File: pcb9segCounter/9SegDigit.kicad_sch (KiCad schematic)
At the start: 10 parts

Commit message: Making progress, figuring out microcontroller interfacing
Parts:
- renumbered D2 to D19, D3 to D20, D4 to D21, D5 to D22, D6 to D23, D7 to D24, D8 to D25, D9 to D26, D10 to D27, D1 to S3
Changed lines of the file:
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@@
 		(dnp no)
 		(fields_autoplaced yes)
-		(property "Reference" "D5"
+		(property "Reference" "D22"
 			(at 104.14 101.6314 0)
 			(effects
@@
 		(instances
 			(project "pcb9segCounter"
+				(path "/c50b0073-6340-498a-8f0c-212ef3b3c0fe/22bfc2a0-8fcb-4720-a36c-753b0c572d0f"
+					(reference "D22")
+					(unit 1)
+				)
+				(path "/c50b0073-6340-498a-8f0c-212ef3b3c0fe/3b31bf75-0830-4091-8274-a65747ea74f2"
+					(reference "D13")
+					(unit 1)
+				)
 				(path "/c50b0073-6340-498a-8f0c-212ef3b3c0fe/5c493882-1689-4a6d-b4b4-08608e8edf66"
-					(reference "D5")
+					(reference "D4")
+					(unit 1)
+				)
+				(path "/c50b0073-6340-498a-8f0c-212ef3b3c0fe/b6b935bf-feab-4172-8fa2-42984df36767"
+					(reference "D31")
 					(unit 1)
 				)
@@
 		(dnp no)
 		(fields_autoplaced yes)
-		(property "Reference" "D4"
+		(property "Reference" "D21"
 			(at 86.36 101.6314 0)
 			(effects
@@
 		(instances
 			(project "pcb9segCounter"
+				(path "/c50b0073-6340-498a-8f0c-212ef3b3c0fe/22bfc2a0-8fcb-4720-a36c-753b0c572d0f"
+					(reference "D21")
+					(unit 1)
+				)
+				(path "/c50b0073-6340-498a-8f0c-212ef3b3c0fe/3b31bf75-0830-4091-8274-a65747ea74f2"
+					(reference "D12")
+					(unit 1)
+				)
 				(path "/c50b0073-6340-498a-8f0c-212ef3b3c0fe/5c493882-1689-4a6d-b4b4-08608e8edf66"
-					(reference "D4")
+					(reference "D3")
+					(unit 1)
+				)
+				(path "/c50b0073-6340-498a-8f0c-212ef3b3c0fe/b6b935bf-feab-4172-8fa2-42984df36767"
+					(reference "D30")
 					(unit 1)
 				)
@@
 		(dnp no)
 		(fields_autoplaced yes)
-		(property "Reference" "D6"
+		(property "Reference" "D23"
 			(at 121.92 101.6314 0)
 			(effects
@@
 		(instances
 			(project "pcb9segCounter"
+				(path "/c50b0073-6340-498a-8f0c-212ef3b3c0fe/22bfc2a0-8fcb-4720-a36c-753b0c572d0f"
+					(reference "D23")
+					(unit 1)
+				)
+				(path "/c50b0073-6340-498a-8f0c-212ef3b3c0fe/3b31bf75-0830-4091-8274-a65747ea74f2"
+					(reference "D14")
+					(unit 1)
+				)
 				(path "/c50b0073-6340-498a-8f0c-212ef3b3c0fe/5c493882-1689-4a6d-b4b4-08608e8edf66"
-					(reference "D6")
+					(reference "D5")
+					(unit 1)
+				)
+				(path "/c50b0073-6340-498a-8f0c-212ef3b3c0fe/b6b935bf-feab-4172-8fa2-42984df36767"
+					(reference "D32")
 					(unit 1)
 				)
@@
 		(dnp no)
 		(fields_autoplaced yes)
-		(property "Reference" "D3"
+		(property "Reference" "D20"
 			(at 68.58 101.6314 0)
 			(effects
@@
 		(instances
 			(project "pcb9segCounter"
+				(path "/c50b0073-6340-498a-8f0c-212ef3b3c0fe/22bfc2a0-8fcb-4720-a36c-753b0c572d0f"
+					(reference "D20")
+					(unit 1)
+				)
+				(path "/c50b0073-6340-498a-8f0c-212ef3b3c0fe/3b31bf75-0830-4091-8274-a65747ea74f2"
+					(reference "D11")
+					(unit 1)
+				)
 				(path "/c50b0073-6340-498a-8f0c-212ef3b3c0fe/5c493882-1689-4a6d-b4b4-08608e8edf66"
-					(reference "D3")
+					(reference "D2")
+					(unit 1)
+				)
+				(path "/c50b0073-6340-498a-8f0c-212ef3b3c0fe/b6b935bf-feab-4172-8fa2-42984df36767"
+					(reference "D29")
 					(unit 1)
 				)
@@
 		(on_board yes)
 		(dnp no)
-		(property "Reference" "D2"
+		(property "Reference" "D19"
 			(at 47.752 99.314 0)
 			(effects
@@
 		(instances
 			(project "pcb9segCounter"
+				(path "/c50b0073-6340-498a-8f0c-212ef3b3c0fe/22bfc2a0-8fcb-4720-a36c-753b0c572d0f"
+					(reference "D19")
+					(unit 1)
+				)
+				(path "/c50b0073-6340-498a-8f0c-212ef3b3c0fe/3b31bf75-0830-4091-8274-a65747ea74f2"
+					(reference "D10")
+					(unit 1)
+				)
 				(path "/c50b0073-6340-498a-8f0c-212ef3b3c0fe/5c493882-1689-4a6d-b4b4-08608e8edf66"
-					(reference "D2")
+					(reference "D1")
+					(unit 1)
+				)
+				(path "/c50b0073-6340-498a-8f0c-212ef3b3c0fe/b6b935bf-feab-4172-8fa2-42984df36767"
+					(reference "D28")
 					(unit 1)
 				)
@@
 		(dnp no)
 		(fields_autoplaced yes)
-		(property "Reference" "D7"
+		(property "Reference" "D24"
 			(at 139.7 101.6314 0)
 			(effects
@@
 		(instances
 			(project "pcb9segCounter"
+				(path "/c50b0073-6340-498a-8f0c-212ef3b3c0fe/22bfc2a0-8fcb-4720-a36c-753b0c572d0f"
+					(reference "D24")
+					(unit 1)
+				)
+				(path "/c50b0073-6340-498a-8f0c-212ef3b3c0fe/3b31bf75-0830-4091-8274-a65747ea74f2"
+					(reference "D15")
+					(unit 1)
+				)
 				(path "/c50b0073-6340-498a-8f0c-212ef3b3c0fe/5c493882-1689-4a6d-b4b4-08608e8edf66"
-					(reference "D7")
+					(reference "D6")
+					(unit 1)
+				)
+				(path "/c50b0073-6340-498a-8f0c-212ef3b3c0fe/b6b935bf-feab-4172-8fa2-42984df36767"
+					(reference "D33")
 					(unit 1)
 				)
@@
 		(dnp no)
 		(fields_autoplaced yes)
-		(property "Reference" "D1"
+		(property "Reference" "S3"
 			(at 101.6 76.8349 0)
 			(effects
@@
 		(instances
 			(project "pcb9segCounter"
+				(path "/c50b0073-6340-498a-8f0c-212ef3b3c0fe/22bfc2a0-8fcb-4720-a36c-753b0c572d0f"
+					(reference "S3")
+					(unit 1)
+				)
+				(path "/c50b0073-6340-498a-8f0c-212ef3b3c0fe/3b31bf75-0830-4091-8274-a65747ea74f2"
+					(reference "S2")
+					(unit 1)
+				)
 				(path "/c50b0073-6340-498a-8f0c-212ef3b3c0fe/5c493882-1689-4a6d-b4b4-08608e8edf66"
-					(reference "D1")
+					(reference "S1")
+					(unit 1)
+				)
+				(path "/c50b0073-6340-498a-8f0c-212ef3b3c0fe/b6b935bf-feab-4172-8fa2-42984df36767"
+					(reference "S4")
 					(unit 1)
 				)
@@
 		(dnp no)
 		(fields_autoplaced yes)
-		(property "Reference" "D10"
+		(property "Reference" "D27"
 			(at 193.04 101.6314 0)
 			(effects
@@
 		(instances
 			(project "pcb9segCounter"
+				(path "/c50b0073-6340-498a-8f0c-212ef3b3c0fe/22bfc2a0-8fcb-4720-a36c-753b0c572d0f"
+					(reference "D27")
+					(unit 1)
+				)
+				(path "/c50b0073-6340-498a-8f0c-212ef3b3c0fe/3b31bf75-0830-4091-8274-a65747ea74f2"
+					(reference "D18")
+					(unit 1)
+				)
 				(path "/c50b0073-6340-498a-8f0c-212ef3b3c0fe/5c493882-1689-4a6d-b4b4-08608e8edf66"
-					(reference "D10")
+					(reference "D9")
+					(unit 1)
+				)
+				(path "/c50b0073-6340-498a-8f0c-212ef3b3c0fe/b6b935bf-feab-4172-8fa2-42984df36767"
+					(reference "D36")
 					(unit 1)
 				)
@@
 		(dnp no)
 		(fields_autoplaced yes)
-		(property "Reference" "D8"
+		(property "Reference" "D25"
 			(at 157.48 101.6314 0)
 			(effects
@@
 		(instances
 			(project "pcb9segCounter"
+				(path "/c50b0073-6340-498a-8f0c-212ef3b3c0fe/22bfc2a0-8fcb-4720-a36c-753b0c572d0f"
+					(reference "D25")
+					(unit 1)
+				)
+				(path "/c50b0073-6340-498a-8f0c-212ef3b3c0fe/3b31bf75-0830-4091-8274-a65747ea74f2"
+					(reference "D16")
+					(unit 1)
+				)
 				(path "/c50b0073-6340-498a-8f0c-212ef3b3c0fe/5c493882-1689-4a6d-b4b4-08608e8edf66"
-					(reference "D8")
+					(reference "D7")
+					(unit 1)
+				)
+				(path "/c50b0073-6340-498a-8f0c-212ef3b3c0fe/b6b935bf-feab-4172-8fa2-42984df36767"
+					(reference "D34")
 					(unit 1)
 				)
@@
 		(dnp no)
 		(fields_autoplaced yes)
-		(property "Reference" "D9"
+		(property "Reference" "D26"
 			(at 175.26 101.6314 0)
 			(effects
@@
 		(instances
 			(project "pcb9segCounter"
+				(path "/c50b0073-6340-498a-8f0c-212ef3b3c0fe/22bfc2a0-8fcb-4720-a36c-753b0c572d0f"
+					(reference "D26")
+					(unit 1)
+				)
+				(path "/c50b0073-6340-498a-8f0c-212ef3b3c0fe/3b31bf75-0830-4091-8274-a65747ea74f2"
+					(reference "D17")
+					(unit 1)
+				)
 				(path "/c50b0073-6340-498a-8f0c-212ef3b3c0fe/5c493882-1689-4a6d-b4b4-08608e8edf66"
-					(reference "D9")
-					(unit 1)
-				)
+					(reference "D8")
+					(unit 1)
+				)
+				(path "/c50b0073-6340-498a-8f0c-212ef3b3c0fe/b6b935bf-feab-4172-8fa2-42984df36767"
+					(reference "D35")
+					(unit 1)
+				)

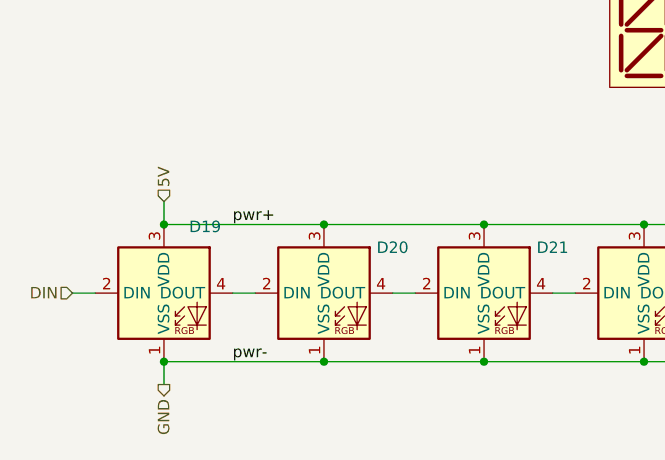
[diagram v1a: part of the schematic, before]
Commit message: Schematic looks good, going to branch to reduce the number of digits from 4 to 2
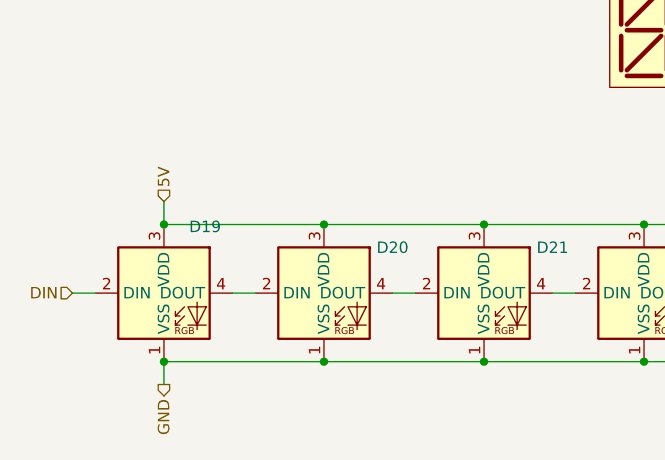
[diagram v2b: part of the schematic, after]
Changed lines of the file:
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@@
-		)
-	)
-	(label "pwr+"
-		(at 50.8 99.06 0)
-		(fields_autoplaced yes)
-		(effects
-			(font
-				(size 1.27 1.27)
-			)
-			(justify left bottom)
-		)
-	)
-	(label "pwr-"
-		(at 50.8 114.3 0)
-		(fields_autoplaced yes)
-		(effects
-			(font
-				(size 1.27 1.27)
-			)
-			(justify left bottom)
 		)
 	)

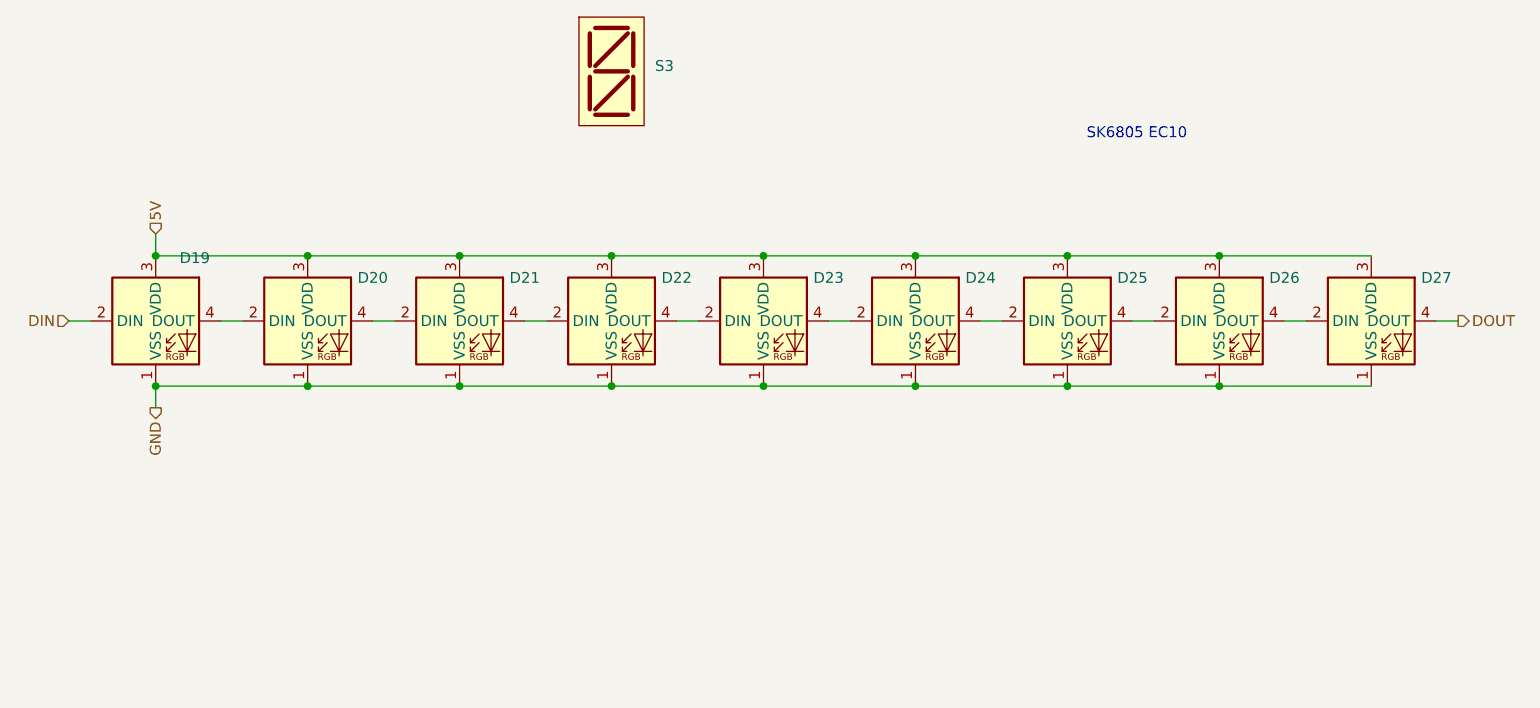
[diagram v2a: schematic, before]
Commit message: reduced to 2 digits, added capacitors
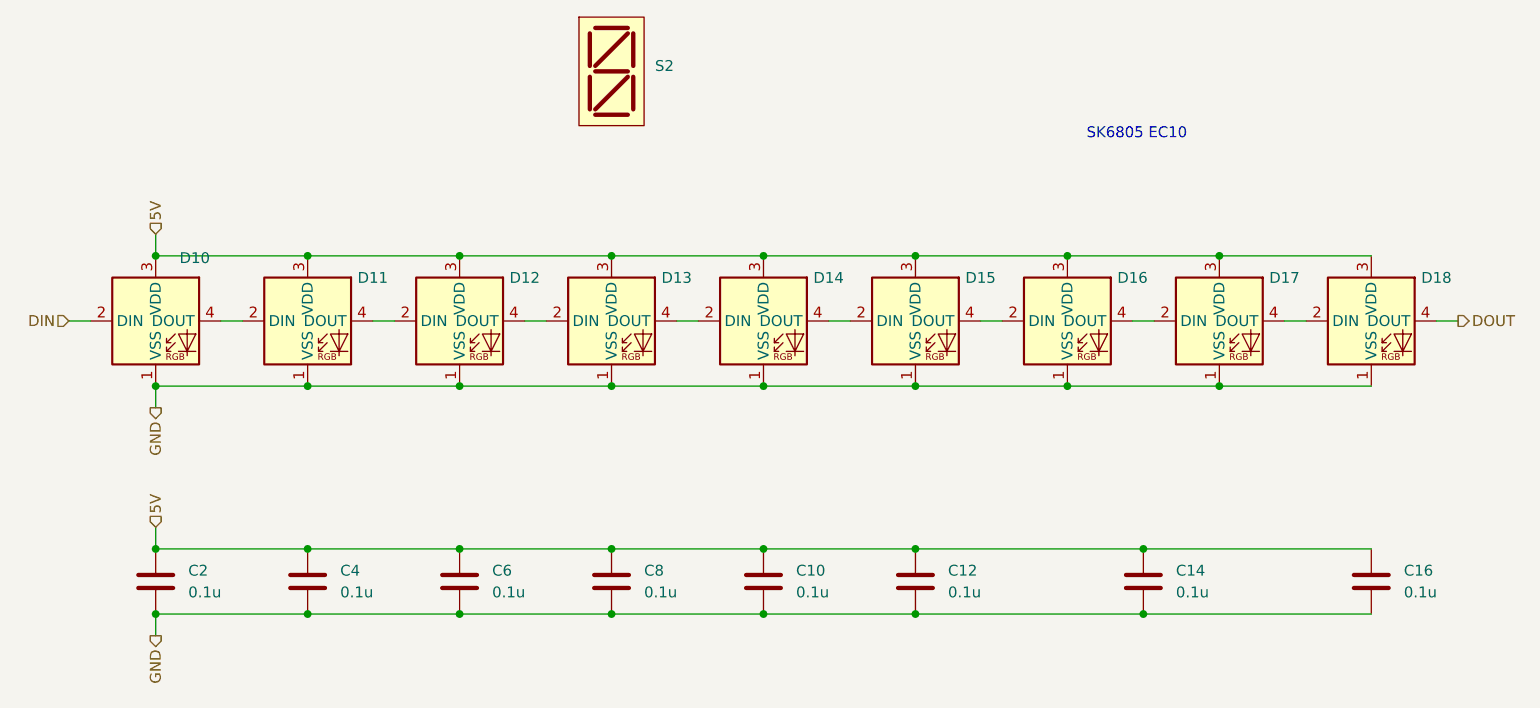
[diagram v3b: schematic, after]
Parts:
- added C10, C12, C14, C16, C2, C4, C6, C8: 0.1u, Capacitor_SMD:C_0805_2012Metric, symbol Device:C
- renumbered D19 to D10, D20 to D11, D21 to D12, D22 to D13, D23 to D14, D24 to D15, D25 to D16, D26 to D17, D27 to D18, S3 to S2
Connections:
- net 5V: now also C10.1, C12.1, C14.1, C16.1, C2.1, C4.1, C6.1, C8.1
- net GND: now also C10.2, C12.2, C14.2, C16.2, C2.2, C4.2, C6.2, C8.2

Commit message: good routing, need to add slikscreen details
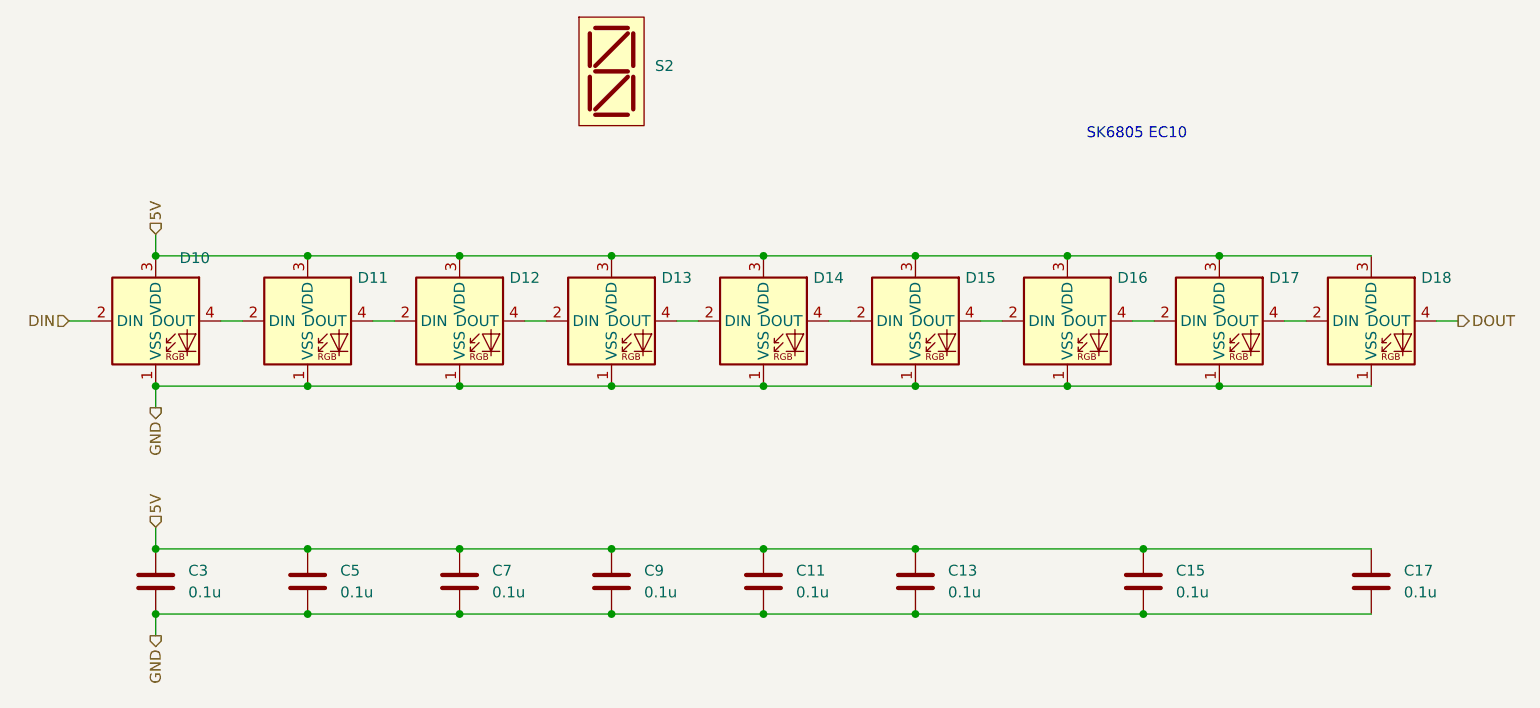
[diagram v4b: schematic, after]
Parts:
- renumbered C10 to C11, C12 to C13, C14 to C15, C16 to C17, C2 to C3, C4 to C5, C6 to C7, C8 to C9
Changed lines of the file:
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@@
 		(on_board yes)
 		(dnp no)
-		(property "Reference" "C2"
+		(property "Reference" "C3"
 			(at 46.99 135.8899 0)
 			(effects
@@
 		(dnp no)
 		(fields_autoplaced yes)
-		(property "Reference" "C14"
+		(property "Reference" "C15"
 			(at 162.56 135.8899 0)
 			(effects
@@
 		(dnp no)
 		(fields_autoplaced yes)
-		(property "Reference" "C10"
+		(property "Reference" "C11"
 			(at 118.11 135.8899 0)
 			(effects
@@
 		(dnp no)
 		(fields_autoplaced yes)
-		(property "Reference" "C12"
+		(property "Reference" "C13"
 			(at 135.89 135.8899 0)
 			(effects
@@
 		(dnp no)
 		(fields_autoplaced yes)
-		(property "Reference" "C4"
+		(property "Reference" "C5"
 			(at 64.77 135.8899 0)
 			(effects
@@
 		(dnp no)
 		(fields_autoplaced yes)
-		(property "Reference" "C16"
+		(property "Reference" "C17"
 			(at 189.23 135.8899 0)
 			(effects
@@
 		(dnp no)
 		(fields_autoplaced yes)
-		(property "Reference" "C6"
+		(property "Reference" "C7"
 			(at 82.55 135.8899 0)
 			(effects
@@
 		(dnp no)
 		(fields_autoplaced yes)
-		(property "Reference" "C8"
+		(property "Reference" "C9"
 			(at 100.33 135.8899 0)
 			(effects

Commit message: Looks really good, all footprints and implementation check out. Looking to move an LED and adding an additional decap capacitor
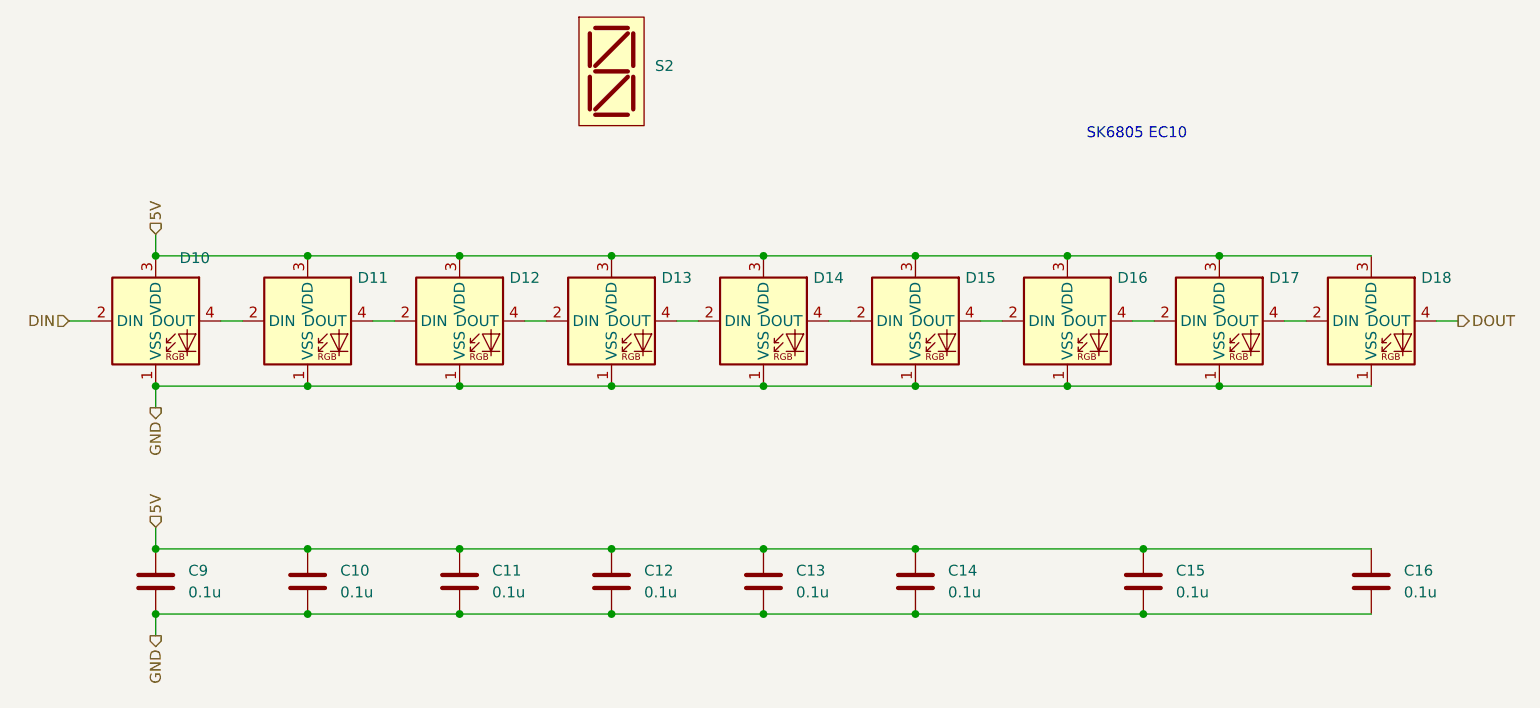
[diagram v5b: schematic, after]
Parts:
- C10: renamed from C5; footprintCheck (none) -> y; implementationCheck (none) -> y
- C11: renamed from C7; footprintCheck (none) -> y; implementationCheck (none) -> y
- C12: renamed from C9; footprintCheck (none) -> y; implementationCheck (none) -> y
- C13: renamed from C11; footprintCheck (none) -> y; implementationCheck (none) -> y
- C14: renamed from C13; footprintCheck (none) -> y; implementationCheck (none) -> y
- C15, D10, D11, D12, D13, D14, D15, D16, D17, D18: footprintCheck (none) -> y; implementationCheck (none) -> y
- C16: renamed from C17; footprintCheck (none) -> y; implementationCheck (none) -> y
- C9: renamed from C3; footprintCheck (none) -> y; implementationCheck (none) -> y
